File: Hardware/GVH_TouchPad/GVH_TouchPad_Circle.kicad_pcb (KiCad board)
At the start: 2 copper layers, 69.3 x 69.3 mm, 5 parts, among them J1 Conn_01x01, J2 Conn_01x01, J4 Conn_01x01, J5 Conn_01x01

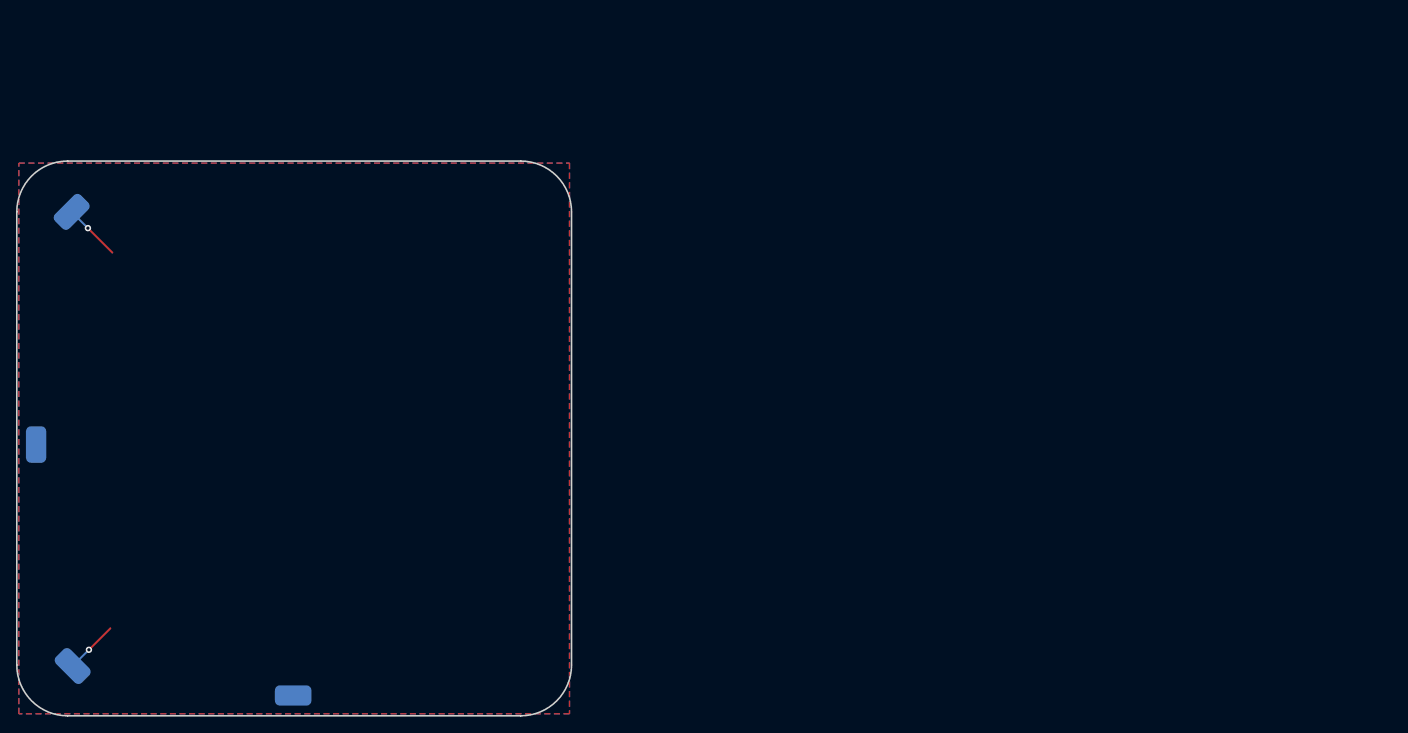
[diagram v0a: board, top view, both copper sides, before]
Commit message: Finished another layout. This is probably the one.
Also  finished the touch pad layouts
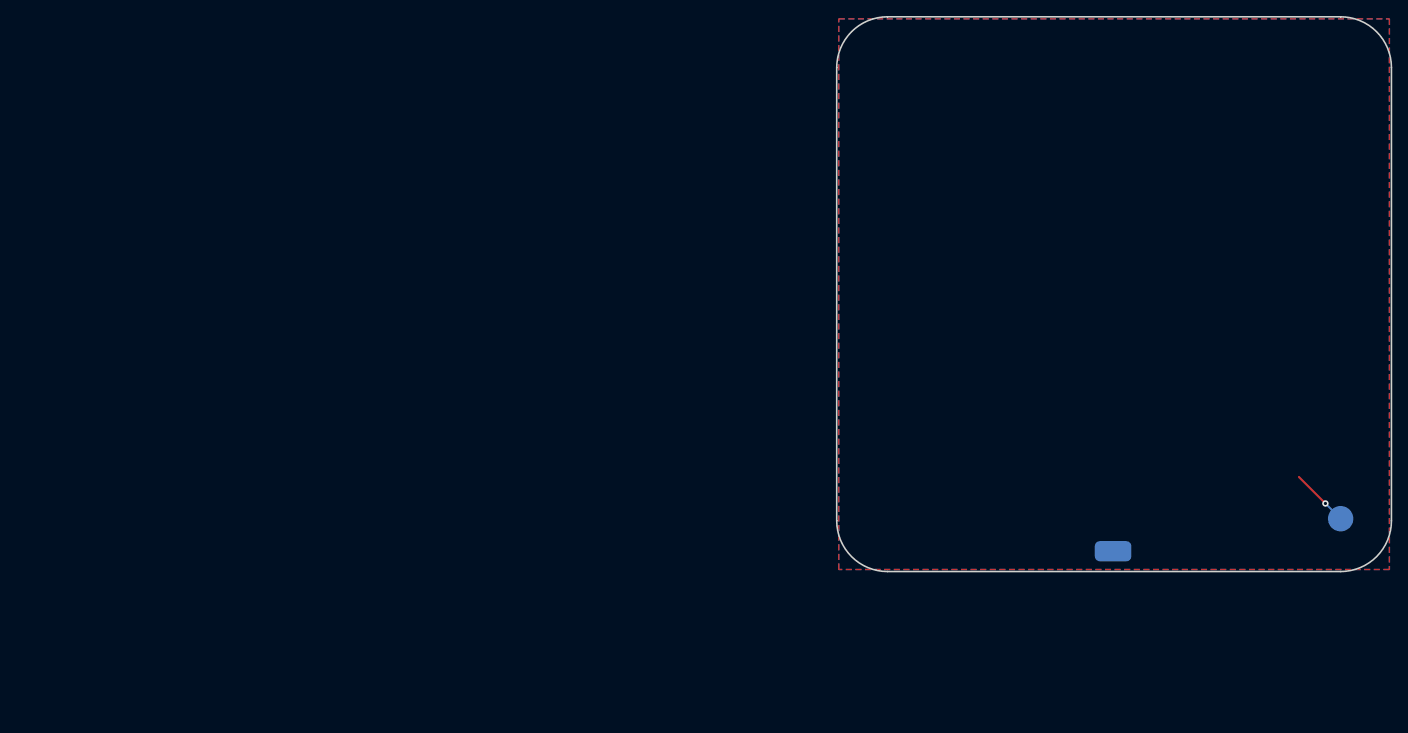
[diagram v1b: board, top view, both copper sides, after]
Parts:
- removed J1, J4: Conn_01x01, 0_touch_pad:SMD_Pad
- added G***: LOGO, 0_logo:MW_Logo_Horizontal_1.0inch, B.Cu at (238.4, 83.2)
- moved J5 163.2 mm to (266.8, 95.2)
- moved J2 135.3 mm to (238.4, 99.3), turned to 180 degrees
- moved REF** 103.9 mm to (238.3, 40.2)
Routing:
- net TOUCH: track 13.8 -> 7.36 mm, vias 2 -> 1

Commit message: Layouts done and ordered.
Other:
- board text added: "GVH • Circle Cap Touch Pad • V0.1 Daniel Bornhorst • 12/2024"
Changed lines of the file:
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@@
   (gr_arc (start 273.177 95.504) (mid 271.317128 99.994128) (end 266.827 101.854)
     (stroke (width 0.2) (type solid)) (layer "Edge.Cuts"))
+  (gr_text "GVH • Circle Cap Touch Pad • V0.1\nDaniel Bornhorst • 12/2024" (at 237.998 88.9) (layer "B.SilkS")
+    (effects (font (size 1.016 1.016) (thickness 0.254) bold) (justify bottom mirror))
+  )
   (segment (start 264.922 93.345) (end 261.62 90.043) (width 0.254) (layer "F.Cu") (net 2))
   (via (at 264.922 93.345) (size 0.8) (drill 0.4) (layers "F.Cu" "B.Cu") (net 2))
